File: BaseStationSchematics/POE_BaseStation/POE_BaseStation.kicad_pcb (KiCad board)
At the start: 2 copper layers, 3 parts, among them J1 Conn_01x10_Socket, J2 Conn_01x10_Socket, U1 Ra01_Breakout_Module-Ra01_Bre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

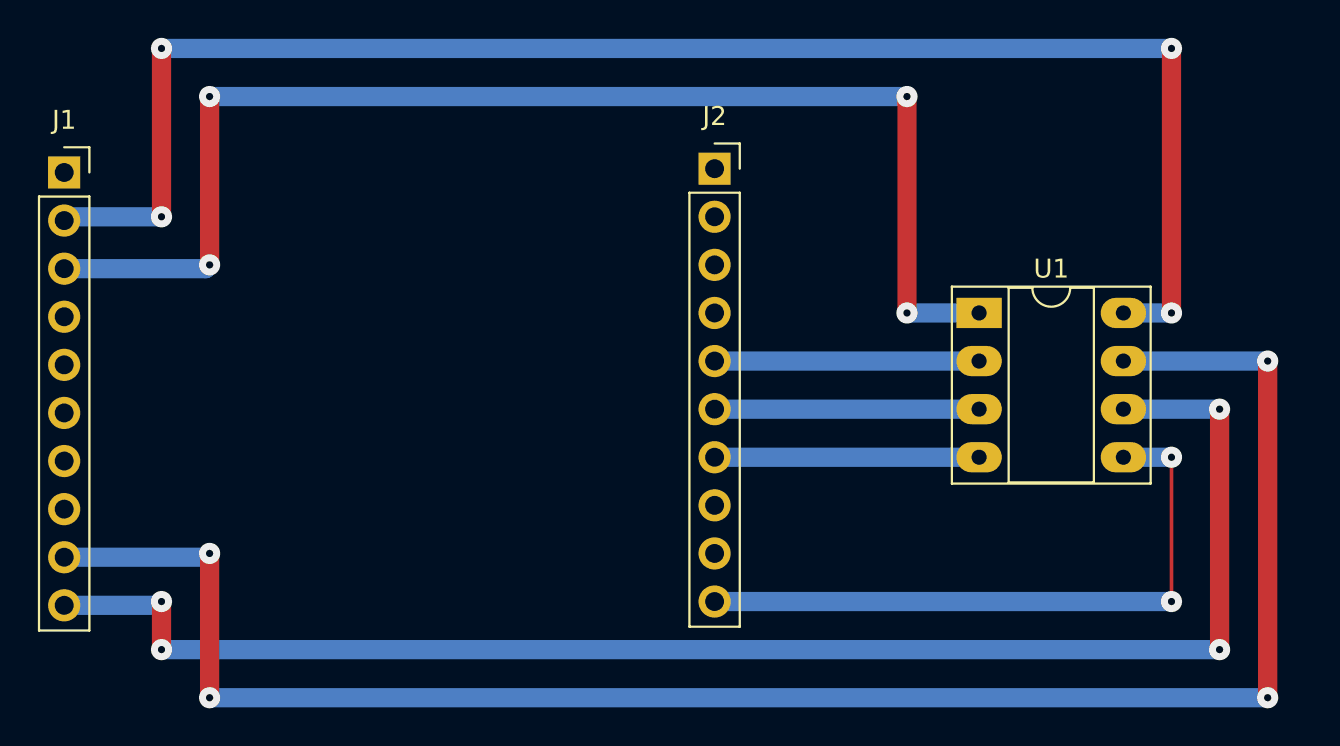
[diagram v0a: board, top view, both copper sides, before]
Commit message: Schematic and board layout matches POE, started adding ethernet support
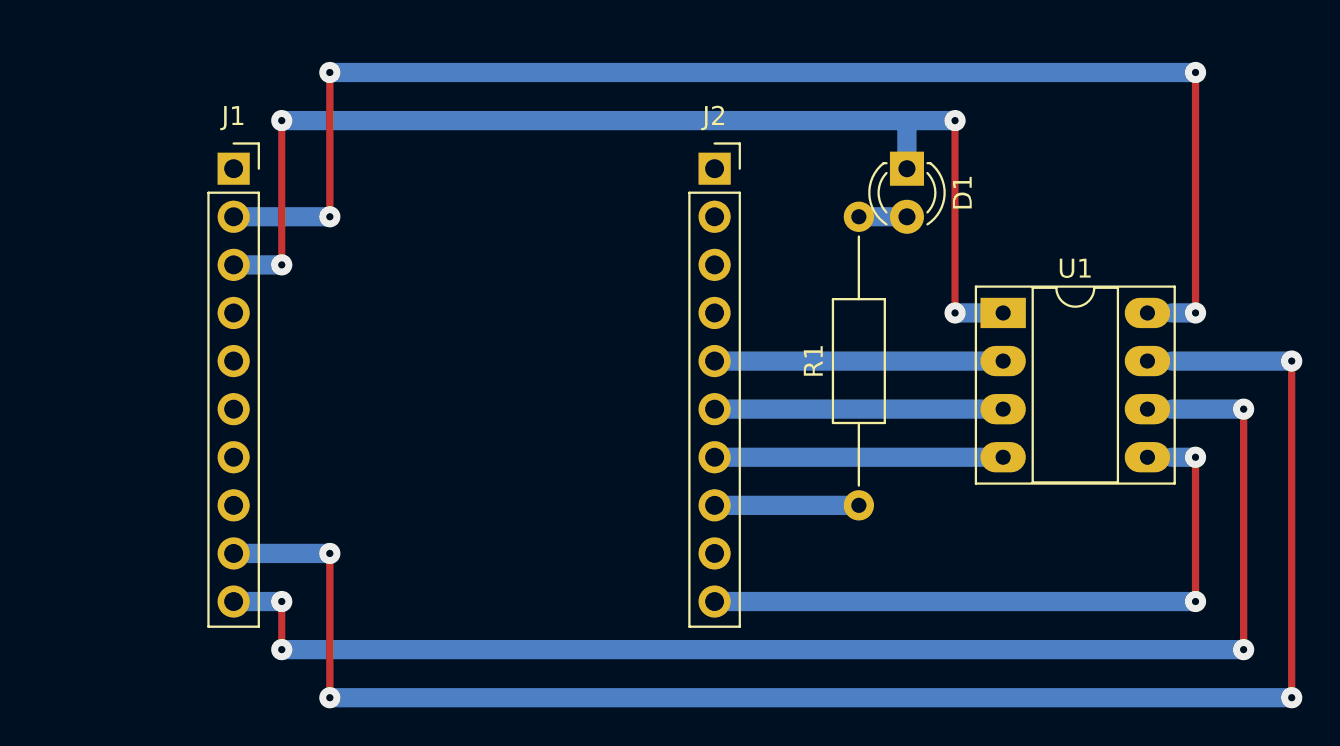
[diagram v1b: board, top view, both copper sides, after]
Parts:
- added D1: LED, LED_THT:LED_D3.0mm, F.Cu at (193.0, 72.4)
- added R1: 220, Resistor_THT:R_Axial_DIN0207_L6.3mm_D2.5mm_P15.24mm_Horizontal, F.Cu at (190.5, 90.2)
- J1: value Conn_01x10_Socket -> Olimex ESP32-POE
- moved J1 8.95 mm to (157.5, 72.4)
- moved U1 1.27 mm to (198.1, 80.0)
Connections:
- J2 pad 8: unconnected-(J2-Pin_8-Pad8) -> /GPIO15
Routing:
- net /+3.3V: track 84.0 -> 72.7 mm
- net /GPIO5: track 81.4 -> 72.4 mm
- net /GPIO4: track 96.7 -> 87.6 mm
- net /GND: track 68.7 -> 61.0 mm
- net /GPIO15: track 0.00 -> 7.62 mm
- net Net-(D1-A): track 0.00 -> 2.54 mm
- net /GPIO33: track 14.0 -> 15.2 mm
- net /GPIO32: track 14.0 -> 15.2 mm
- net /GPIO16: track 14.0 -> 15.2 mm
